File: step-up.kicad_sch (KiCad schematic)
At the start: 22 parts, among them Q22 NMOS, U15 LM34966

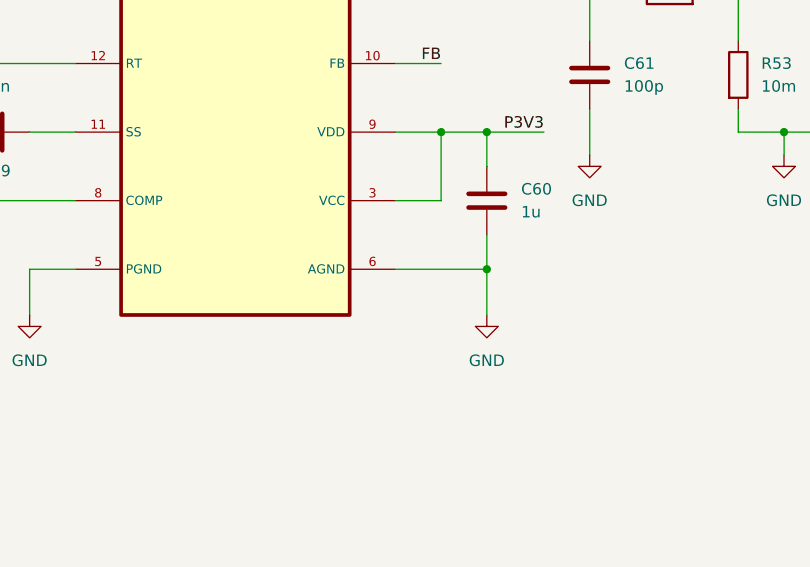
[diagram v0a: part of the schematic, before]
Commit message: ready schematic for layout
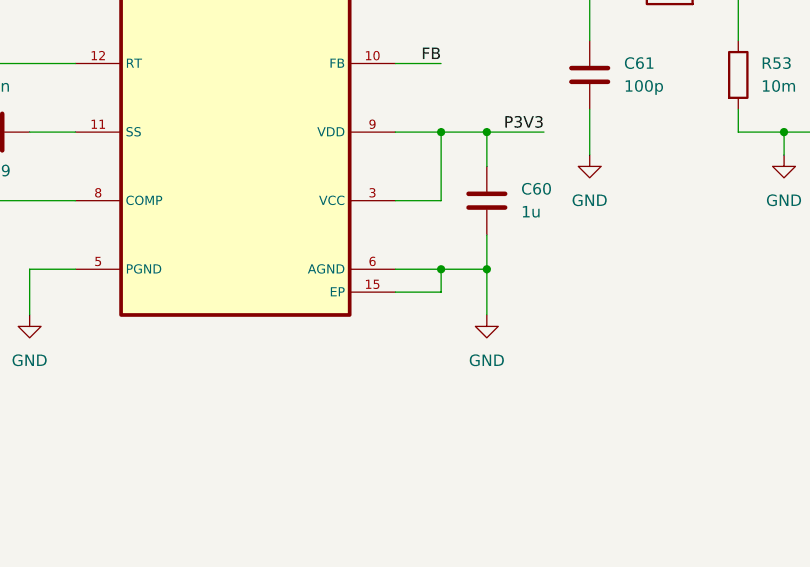
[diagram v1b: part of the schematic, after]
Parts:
- L2: footprint (none) -> Inductor_SMD:L_Bourns-SRN8040_8x8.15mm
- R55, R56, R57: footprint (none) -> Resistor_SMD:R_0603_1608Metric_Pad0.98x0.95mm_HandSolder
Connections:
- net GND: now also U15.15 (EP)
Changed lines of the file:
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@@
+	)
+	(junction
+		(at 162.56 121.92)
+		(diameter 0)
+		(color 0 0 0 0)
 	)
 	(junction
@@
 	(wire
 		(pts
-			(xy 167.64 121.92) (xy 157.48 121.92)
+			(xy 167.64 121.92) (xy 162.56 121.92)
 		)
 		(stroke
@@
 	(wire
 		(pts
+			(xy 162.56 121.92) (xy 157.48 121.92)
+		)
+		(stroke
+			(width 0)
+			(type default)
+		)
+	)
+	(wire
+		(pts
 			(xy 181.61 76.2) (xy 182.88 76.2)
 		)
@@
 	(wire
 		(pts
+			(xy 162.56 124.46) (xy 162.56 121.92)
+		)
+		(stroke
+			(width 0)
+			(type default)
+		)
+	)
+	(wire
+		(pts
 			(xy 195.58 91.44) (xy 200.66 91.44)
+		)
+		(stroke
+			(width 0)
+			(type default)
+		)
+	)
+	(wire
+		(pts
+			(xy 157.48 124.46) (xy 162.56 124.46)
 		)
 		(stroke
@@
 			)
 		)
-		(property "Footprint" ""
+		(property "Footprint" "Resistor_SMD:R_0603_1608Metric_Pad0.98x0.95mm_HandSolder"
 			(at 223.012 107.95 90)
 			(effects
@@
 			)
 		)
-		(property "Datasheet" "~"
+		(property "Datasheet" ""
 			(at 224.79 107.95 0)
 			(effects
@@
 		(pin "1"
 		)
+		(pin "15"
+		)
 		(instances
 			(project "ultrasonic_V3_HW"
@@
 			)
 		)
-		(property "Footprint" ""
+		(property "Footprint" "Resistor_SMD:R_0603_1608Metric_Pad0.98x0.95mm_HandSolder"
 			(at 223.012 77.47 90)
 			(effects
@@
 			)
 		)
-		(property "Footprint" ""
+		(property "Footprint" "Resistor_SMD:R_0603_1608Metric_Pad0.98x0.95mm_HandSolder"
 			(at 223.012 90.17 90)
 			(effects
@@
 			)
 		)
-		(property "Footprint" ""
+		(property "Footprint" "Inductor_SMD:L_Bourns-SRN8040_8x8.15mm"
 			(at 139.7 60.96 0)
 			(effects
@@
 			)
 		)
-		(property "Datasheet" "~"
+		(property "Datasheet" "https://cz.mouser.com/ProductDetail/ABRACON/ASPIAIG-S8050-6R8M-T?qs=l%2FgYmo23PNPNrTLXodySdQ%3D%3D"
 			(at 139.7 60.96 0)
 			(effects

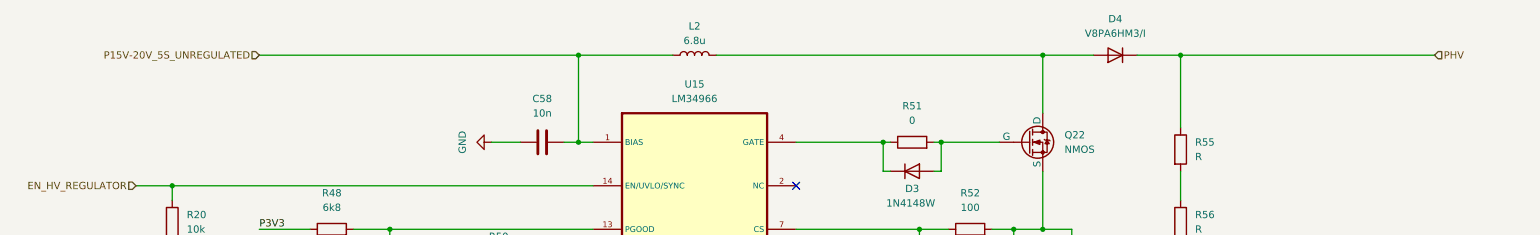
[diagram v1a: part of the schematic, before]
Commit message: schematic ready, basic layout done
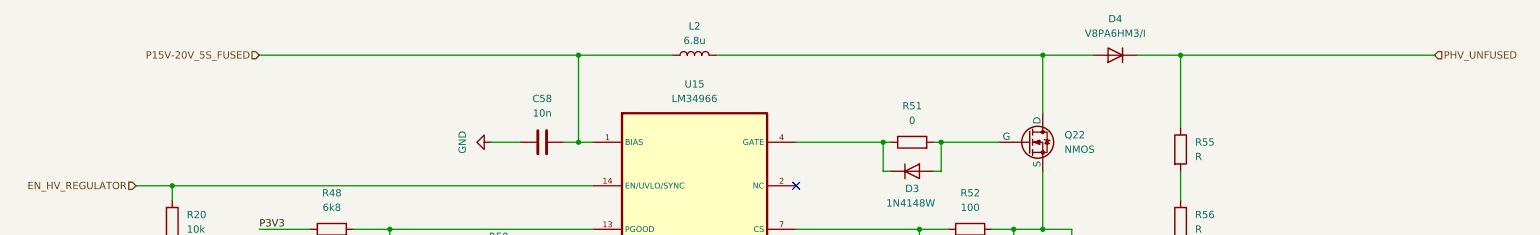
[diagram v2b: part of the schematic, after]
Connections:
- net P15V-20V_5S_UNREGULATED renamed P15V-20V_5S_FUSED
- net PHV renamed PHV_UNFUSED
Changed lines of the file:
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@@
 		)
 	)
-	(hierarchical_label "PHV"
+	(hierarchical_label "PHV_UNFUSED"
 		(shape input)
 		(at 269.24 60.96 0)
@@
 		)
 	)
-	(hierarchical_label "P15V-20V_5S_UNREGULATED"
+	(hierarchical_label "P15V-20V_5S_FUSED"
 		(shape input)
 		(at 63.5 60.96 180)

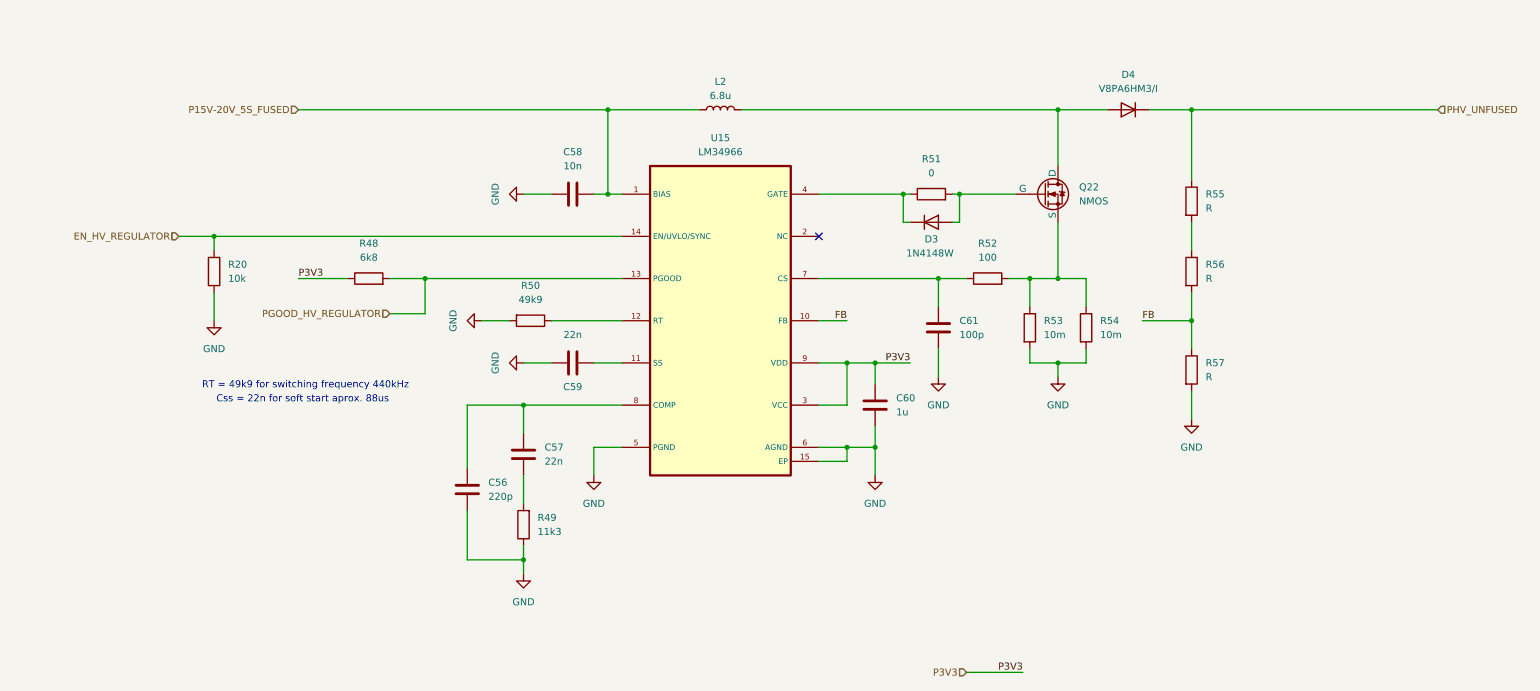
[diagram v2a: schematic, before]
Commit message: no errors schematic, basic routing done
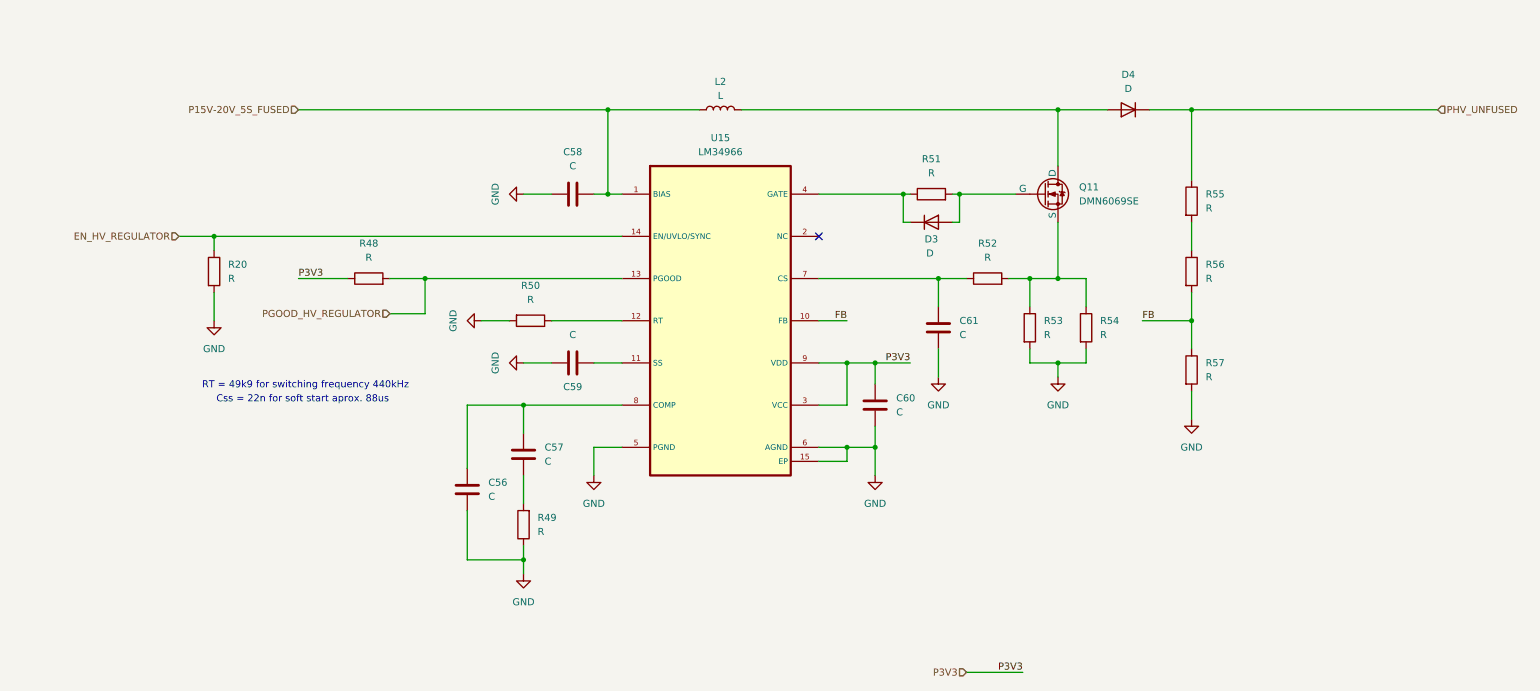
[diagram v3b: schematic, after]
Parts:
- removed Q22: NMOS, Package_TO_SOT_SMD:SOT-223-3_TabPin2, symbol Simulation_SPICE:NMOS
- added Q11: DMN6069SE, Package_TO_SOT_SMD:SOT-223-3_TabPin2, symbol 10_ICs:DMN6069SE
- C56: value 220p -> C
- C57, C59: value 22n -> C
- C58: value 10n -> C
- C60: value 1u -> C
- C61: value 100p -> C
- D3: value 1N4148W -> D
- D4: value V8PA6HM3/I -> D
- L2: value 6.8u -> L
- R20: value 10k -> R
- R48: value 6k8 -> R
- R49: value 11k3 -> R
- R50: value 49k9 -> R
- R51: value 0 -> R
- R52: value 100 -> R
- R53, R54: value 10m -> R
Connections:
- net at R52.2, R53.1, R54.1: now also Q11.3 (S)
- net at D3.2 (A), R51.2: now also Q11.1 (G)
- net at D4.2 (A), L2.2: now also Q11.2 (D)
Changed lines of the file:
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@@
 			)
 		)
-		(property "Value" "22n"
+		(property "Value" "C"
 			(at 113.03 101.6 90)
 			(effects
@@
 			)
 		)
-		(property "Value" "10m"
+		(property "Value" "R"
 			(at 198.12 101.5999 0)
 			(effects
@@
 			)
 		)
-		(property "Datasheet" "https://eu.mouser.com/ProductDetail/Bussmann-Eaton/MFL0603R0100FA?qs=sGAEpiMZZMtlleCFQhR%2FzX%2FMoTUoyF2nsJoSKa0HvBn6AmlRP7WW6Q%3D%3D"
+		(property "Datasheet" "~"
 			(at 195.58 100.33 0)
 			(effects
@@
 			)
 		)
-		(property "Value" "6k8"
+		(property "Value" "R"
 			(at 76.2 87.63 90)
 			(effects
@@
 			)
 		)
-		(property "Value" "10k"
+		(property "Value" "R"
 			(at 50.8 91.4399 0)
 			(effects
@@
 			)
 		)
-		(property "Value" "22n"
+		(property "Value" "C"
 			(at 107.95 124.4599 0)
 			(effects
@@
 			)
 		)
-		(property "Value" "220p"
+		(property "Value" "C"
 			(at 97.79 130.8099 0)
 			(effects
@@
 			)
 		)
-		(property "Value" "0"
+		(property "Value" "R"
 			(at 177.8 72.39 90)
 			(effects
@@
 			)
 		)
-		(property "Datasheet" ""
+		(property "Datasheet" "~"
 			(at 224.79 107.95 0)
 			(effects
@@
 			)
 		)
-		(property "Value" "11k3"
+		(property "Value" "R"
 			(at 106.68 137.1599 0)
 			(effects
@@
 			)
 		)
-		(property "Value" "100p"
+		(property "Value" "C"
 			(at 182.88 101.5999 0)
 			(effects
@@
 			)
 		)
-		(property "Value" "49k9"
+		(property "Value" "R"
 			(at 105.41 95.25 90)
 			(effects
@@
 			)
 		)
-		(property "Value" "V8PA6HM3/I"
+		(property "Value" "D"
 			(at 213.36 57.15 0)
 			(effects
@@
 			)
 		)
-		(property "Datasheet" "https://cz.mouser.com/ProductDetail/Vishay-General-Semiconductor/V8PA6HM3-I?qs=b%252B2mHxW%2Fy4Va%252BzY9SymevA%3D%3D"
+		(property "Datasheet" "~"
 			(at 213.36 60.96 0)
 			(effects
@@
 			)
 		)
-		(property "Value" "10m"
+		(property "Value" "R"
 			(at 208.28 101.5999 0)
 			(effects
@@
 			)
 		)
-		(property "Datasheet" "https://eu.mouser.com/ProductDetail/Bussmann-Eaton/MFL0603R0100FA?qs=sGAEpiMZZMtlleCFQhR%2FzX%2FMoTUoyF2nsJoSKa0HvBn6AmlRP7WW6Q%3D%3D"
+		(property "Datasheet" "~"
 			(at 205.74 100.33 0)
 			(effects
@@
 			)
 		)
-		(property "Value" "1N4148W"
+		(property "Value" "D"
 			(at 177.546 86.868 0)
 			(effects
@@
 			)
 		)
-		(property "Datasheet" "https://cz.mouser.com/ProductDetail/Diodes-Incorporated/1N4148W-7-F?qs=LHX0FizJzg7Ae9ZM8LTAWw%3D%3D&srsltid=AfmBOorMVh9aQCQJXlRmu5q-x4k63j0_Z9czWefQ9uFlGwFx4R5vInln"
+		(property "Datasheet" "~"
 			(at 177.8 81.28 0)
 			(effects
@@
 			)
 		)
-		(property "Value" "100"
+		(property "Value" "R"
 			(at 187.96 87.63 90)
 			(effects
@@
 	)
 	(symbol
-		(lib_id "Simulation_SPICE:NMOS")
-		(at 198.12 76.2 0)
-		(unit 1)
-		(exclude_from_sim no)
-		(in_bom yes)
-		(on_board yes)
-		(dnp no)
-		(fields_autoplaced yes)
-		(property "Reference" "Q22"
-			(at 204.47 74.9299 0)
-			(effects
-				(font
-					(size 1.27 1.27)
-				)
-				(justify left)
-			)
-		)
-		(property "Value" "NMOS"
-			(at 204.47 77.4699 0)
-			(effects
-				(font
-					(size 1.27 1.27)
-				)
-				(justify left)
-			)
-		)
-		(property "Footprint" "Package_TO_SOT_SMD:SOT-223-3_TabPin2"
-			(at 203.2 73.66 0)
-			(effects
-				(font
-					(size 1.27 1.27)
-				)
-				(hide yes)
-			)
-		)
-		(property "Datasheet" "https://cz.mouser.com/ProductDetail/Diodes-Incorporated/DMN6069SE-13?qs=y6ZabgHbY%252BxxJPeGPFEm5g%3D%3D"
-			(at 198.12 88.9 0)
-			(effects
-				(font
-					(size 1.27 1.27)
-				)
-				(hide yes)
-			)
-		)
-		(property "Description" "DMN6069SE-13"
-			(at 198.12 76.2 0)
-			(effects
-				(font
-					(size 1.27 1.27)
-				)
-				(hide yes)
-			)
-		)
-		(property "Sim.Device" "NMOS"
-			(at 198.12 93.345 0)
-			(effects
-				(font
-					(size 1.27 1.27)
-				)
-				(hide yes)
-			)
-		)
-		(property "Sim.Type" "VDMOS"
-			(at 198.12 95.25 0)
-			(effects
-				(font
-					(size 1.27 1.27)
-				)
-				(hide yes)
-			)
-		)
-		(property "Sim.Pins" "1=D 2=G 3=S"
-			(at 198.12 91.44 0)
-			(effects
-				(font
-					(size 1.27 1.27)
-				)
-				(hide yes)
-			)
-		)
-		(pin "2"
-		)
-		(pin "1"
-		)
-		(pin "3"
-		)
-		(instances
-			(project "ultrasonic_V3_HW"
-				(path "/731d4032-cf8d-4f76-95ca-2ec44c8e0816/fa0f0e71-32a1-4f06-ba3c-8552f7539938/20962ebf-4383-4e37-a926-d36c5a815eed"
-					(reference "Q22")
-					(unit 1)
-				)
-			)
-		)
-	)
-	(symbol
 		(lib_id "power:GND")
 		(at 104.14 76.2 270)
@@
 	)
 	(symbol
+		(lib_id "10_ICs:DMN6069SE")
+		(at 193.04 71.12 0)
+		(unit 1)
+		(exclude_from_sim no)
+		(in_bom yes)
+		(on_board yes)
+		(dnp no)
+		(fields_autoplaced yes)
+		(property "Reference" "Q11"
+			(at 204.47 74.9299 0)
+			(effects
+				(font
+					(size 1.27 1.27)
+				)
+				(justify left)
+			)
+		)
+		(property "Value" "DMN6069SE"
+			(at 204.47 77.4699 0)
+			(effects
+				(font
+					(size 1.27 1.27)
+				)
+				(justify left)
+			)
+		)
+		(property "Footprint" "Package_TO_SOT_SMD:SOT-223-3_TabPin2"
+			(at 193.04 71.12 0)
+			(effects
+				(font
+					(size 1.27 1.27)
+				)
+				(hide yes)
+			)
+		)
+		(property "Datasheet" "https://cz.mouser.com/datasheet/2/115/DIODS21240_1-2542003.pdf"
+			(at 193.04 71.12 0)
+			(effects
+				(font
+					(size 1.27 1.27)
+				)
+				(hide yes)
+			)
+		)
+		(property "Description" ""
+			(at 193.04 71.12 0)
+			(effects
+				(font
+					(size 1.27 1.27)
+				)
+				(hide yes)
+			)
+		)
+		(pin "1"
+		)
+		(pin "2"
+		)
+		(pin "3"
+		)
+		(instances
+			(project "ultrasonic_V3_HW"
+				(path "/731d4032-cf8d-4f76-95ca-2ec44c8e0816/fa0f0e71-32a1-4f06-ba3c-8552f7539938/20962ebf-4383-4e37-a926-d36c5a815eed"
+					(reference "Q11")
+					(unit 1)
+				)
+			)
+		)
+	)
+	(symbol
 		(lib_id "Device:L")
 		(at 139.7 60.96 90)
@@
 			)
 		)
-		(property "Value" "6.8u"
+		(property "Value" "L"
 			(at 139.7 58.42 90)
 			(effects
@@
 			)
 		)
-		(property "Datasheet" "https://cz.mouser.com/ProductDetail/ABRACON/ASPIAIG-S8050-6R8M-T?qs=l%2FgYmo23PNPNrTLXodySdQ%3D%3D"
+		(property "Datasheet" "~"
 			(at 139.7 60.96 0)
 			(effects
@@
 			)
 		)
-		(property "Value" "10n"
+		(property "Value" "C"
 			(at 113.03 71.12 90)
 			(effects
@@
 			)
 		)
-		(property "Value" "1u"
+		(property "Value" "C"
 			(at 171.45 115.5699 0)
 			(effects

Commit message: most values in schematic filled corrected footprint mistake
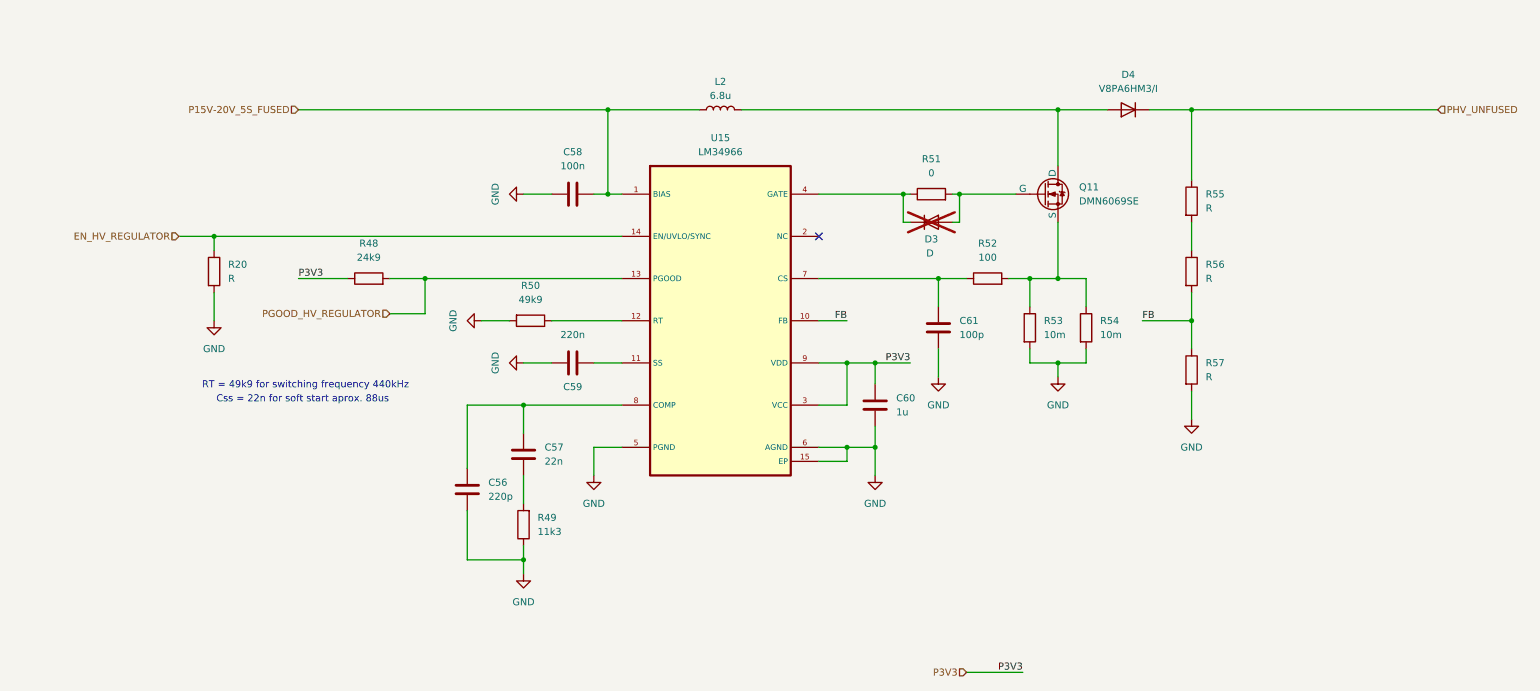
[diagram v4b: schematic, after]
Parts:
- C56: value C -> 220p
- C57: value C -> 22n
- C58: value C -> 100n
- C59: value C -> 220n
- C60: value C -> 1u
- C61: value C -> 100p
- D3: now not fitted
- D4: value D -> V8PA6HM3/I
- L2: value L -> 6.8u
- R48: value R -> 24k9
- R49: value R -> 11k3
- R50: value R -> 49k9
- R51: value R -> 0
- R52: value R -> 100
- R53, R54: value R -> 10m
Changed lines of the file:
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@@
 			)
 		)
-		(property "Value" "C"
+		(property "Value" "220n"
 			(at 113.03 101.6 90)
 			(effects
@@
 			)
 		)
-		(property "Value" "R"
+		(property "Value" "10m"
 			(at 198.12 101.5999 0)
 			(effects
@@
 			)
 		)
-		(property "Datasheet" "~"
+		(property "Datasheet" "https://cz.mouser.com/ProductDetail/Panasonic/ERJ-3BWFR025V?qs=22lEN67Lqx6yyPyD%2FCtjJQ%3D%3D"
 			(at 195.58 100.33 0)
 			(effects
@@
 			)
 		)
-		(property "Value" "R"
+		(property "Value" "24k9"
 			(at 76.2 87.63 90)
 			(effects
@@
 			)
 		)
-		(property "Value" "C"
+		(property "Value" "22n"
 			(at 107.95 124.4599 0)
 			(effects
@@
 			)
 		)
-		(property "Value" "C"
+		(property "Value" "220p"
 			(at 97.79 130.8099 0)
 			(effects
@@
 			)
 		)
-		(property "Value" "R"
+		(property "Value" "0"
 			(at 177.8 72.39 90)
 			(effects
@@
 			)
 		)
-		(property "Value" "R"
+		(property "Value" "11k3"
 			(at 106.68 137.1599 0)
 			(effects
@@
 			)
 		)
-		(property "Datasheet" ""
+		(property "Datasheet" "https://cz.mouser.com/ProductDetail/Texas-Instruments/LM34966QPWPRQ1?qs=zW32dvEIR3tnRgqzlr9chw%3D%3D"
 			(at 127 71.12 0)
 			(effects
@@
 			)
 		)
-		(property "Value" "C"
+		(property "Value" "100p"
 			(at 182.88 101.5999 0)
 			(effects
@@
 			)
 		)
-		(property "Value" "R"
+		(property "Value" "49k9"
 			(at 105.41 95.25 90)
 			(effects
@@
 			)
 		)
-		(property "Value" "D"
+		(property "Value" "V8PA6HM3/I"
 			(at 213.36 57.15 0)
 			(effects
@@
 			)
 		)
-		(property "Datasheet" "~"
+		(property "Datasheet" "https://cz.mouser.com/ProductDetail/Vishay-General-Semiconductor/V8PA6HM3-I?qs=b%252B2mHxW%2Fy4Va%252BzY9SymevA%3D%3D"
 			(at 213.36 60.96 0)
 			(effects
@@
 			)
 		)
-		(property "Value" "R"
+		(property "Value" "10m"
 			(at 208.28 101.5999 0)
 			(effects
@@
 			)
 		)
-		(property "Datasheet" "~"
+		(property "Datasheet" "https://cz.mouser.com/ProductDetail/Panasonic/ERJ-3BWFR025V?qs=22lEN67Lqx6yyPyD%2FCtjJQ%3D%3D"
 			(at 205.74 100.33 0)
 			(effects
@@
 		(in_bom yes)
 		(on_board yes)
-		(dnp no)
+		(dnp yes)
 		(property "Reference" "D3"
 			(at 177.8 84.328 0)
@@
 			)
 		)
-		(property "Value" "R"
+		(property "Value" "100"
 			(at 187.96 87.63 90)
 			(effects
@@
 			)
 		)
-		(property "Value" "L"
+		(property "Value" "6.8u"
 			(at 139.7 58.42 90)
 			(effects
@@
 			)
 		)
-		(property "Datasheet" "~"
+		(property "Datasheet" "https://cz.mouser.com/ProductDetail/Vishay-Dale/IFSC3232DBER6R8M01?qs=dbcCsuKDzFVXQMJFlZnyoQ%3D%3D"
 			(at 139.7 60.96 0)
 			(effects
@@
 			)
 		)
-		(property "Value" "C"
+		(property "Value" "100n"
 			(at 113.03 71.12 90)
 			(effects
@@
 			)
 		)
-		(property "Value" "C"
+		(property "Value" "1u"
 			(at 171.45 115.5699 0)
 			(effects

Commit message: V2 finished
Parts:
- added C113, C116, C117, C63, C96: 100n, Capacitor_SMD:C_0603_1608Metric_Pad1.08x0.95mm_HandSolder, symbol Device:C
- added C114, C115, C15, C62, C94, C95: 10u, Capacitor_SMD:C_0805_2012Metric_Pad1.18x1.45mm_HandSolder, symbol Device:C
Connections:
- net GND: now also C113.2, C114.1, C115.1, C116.2, C117.2, C15.1, C62.1, C63.2, C94.1, C95.1, C96.2
- net P15V-20V_5S_FUSED: now also C113.1, C114.2, C115.2, C116.1, C117.1, C94.2, C95.2, C96.1
- net PHV_UNFUSED: now also C15.2, C62.2, C63.1
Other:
- moved on the sheet: D4, L2
